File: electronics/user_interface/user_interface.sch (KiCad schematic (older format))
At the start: 29 parts, among them J1 Conn_01x06, J2 Conn_02x05_Odd_Even, U1 PCF8574, U2 PCF8574

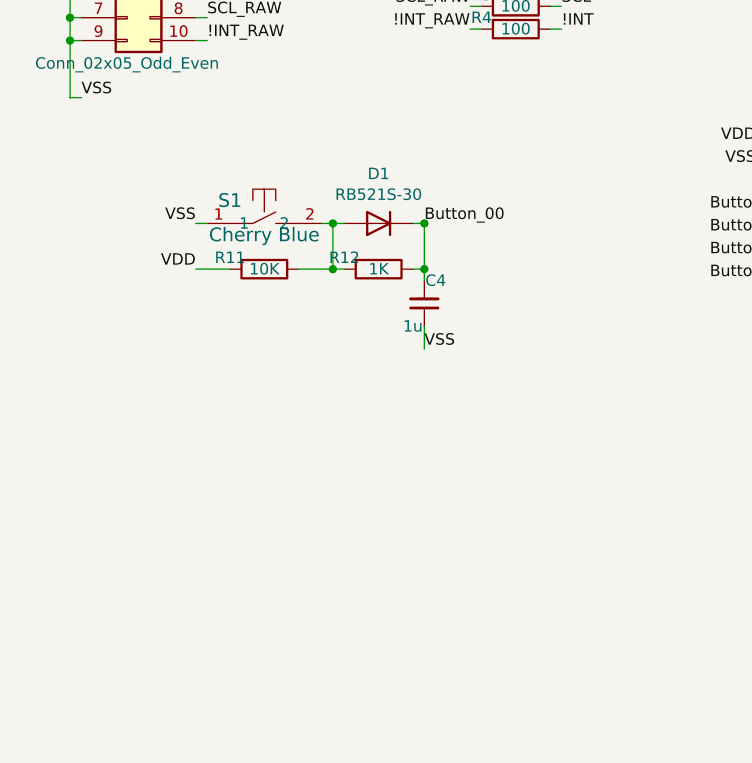
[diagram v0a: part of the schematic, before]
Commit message: added 3 switches extra to schematic
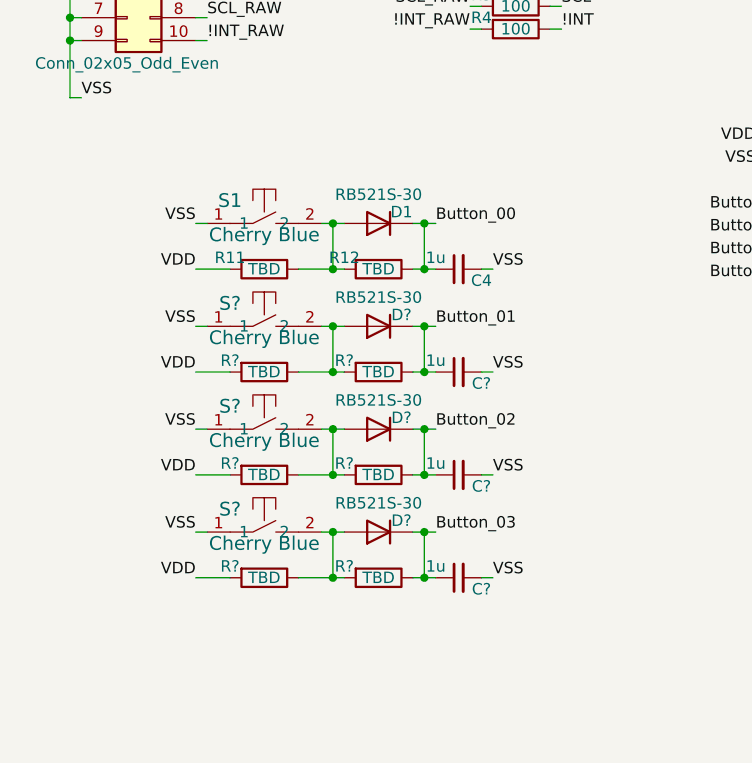
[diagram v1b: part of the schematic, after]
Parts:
- added C? (x3): 1u, SquantorRcl:C_0603, symbol Device:C_Small
- added D? (x3): RB521S-30, SquantorDiodes:SOD-523, symbol Device:D
- added R? (x6): TBD, SquantorRcl:R_0603_hand, symbol Device:R
- added S? (x3): Cherry Blue, MX_Only:MXOnly-1U-NoLED, symbol SquantorSwitches:2pin_tact_switch
- R11: value 10K -> TBD
- R12: value 1K -> TBD
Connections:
- net Button_00: now also C4.1; no longer C4.2
- net Button_01: now also C?.1, D?.1 (K), R?.1
- net Button_02: now also C?.1, D?.1 (K), R?.1
- net Button_03: now also C?.1, D?.1 (K), R?.1
- net VDD: now also R?.2, R?.2, R?.2
- net VSS: now also C4.2, C?.2, C?.2, C?.2, S?.1, S?.1, S?.1; no longer C4.1
- new net: D?.2 (A), R?.1, R?.2, S?.2 (x3)
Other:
- moved on the sheet: C4

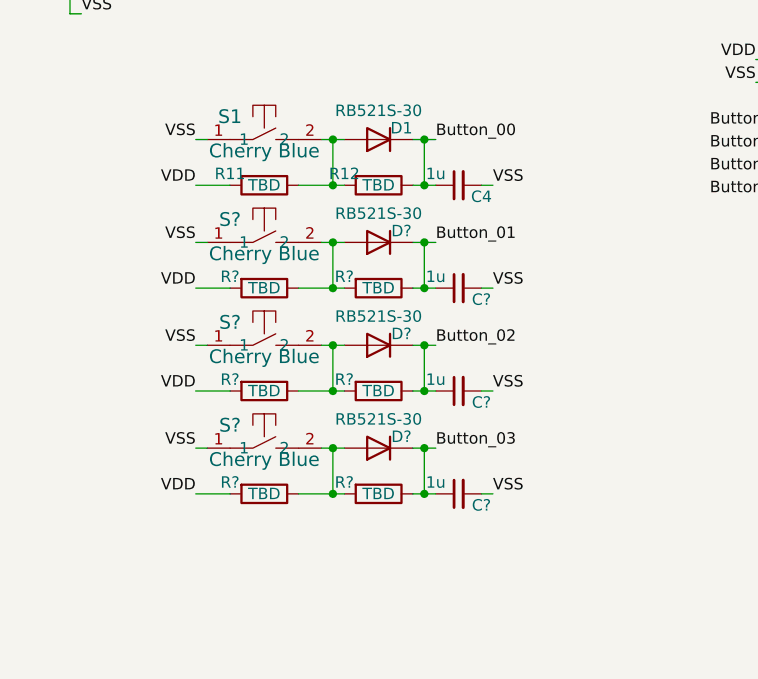
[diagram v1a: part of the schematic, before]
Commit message: minor silk and layout
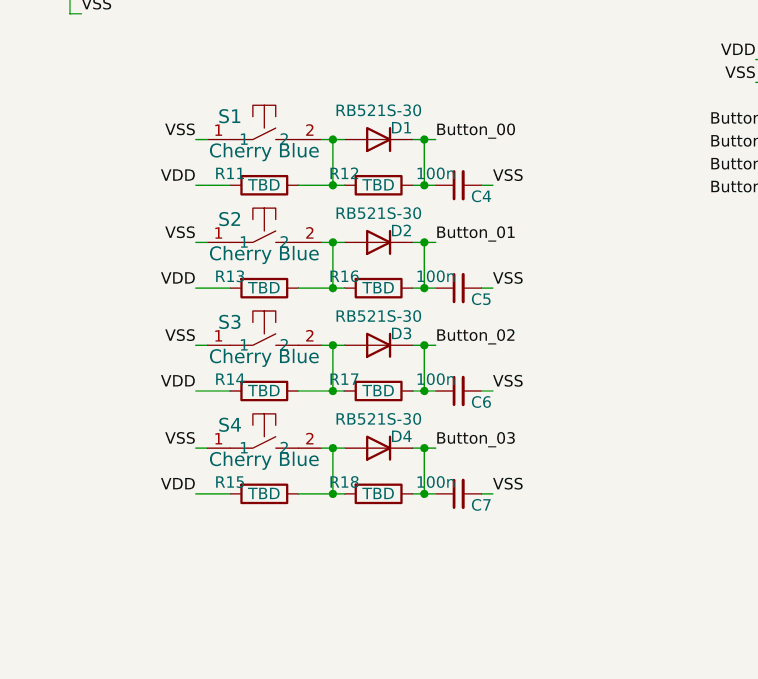
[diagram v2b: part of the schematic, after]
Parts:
- C4: value 1u -> 100n
- C5, C6, C7: renamed from C?; value 1u -> 100n
- gave numbers to parts that had none: 12
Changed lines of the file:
@@
 P 2500 3050
 F 0 "C4" V 2450 2950 50  0000 C CNN
-F 1 "1u" V 2550 3150 50  0000 C CNN
+F 1 "100n" V 2550 3150 50  0000 C CNN
 F 2 "SquantorRcl:C_0603" H 2500 3050 50  0001 C CNN
 F 3 "~" H 2500 3050 50  0001 C CNN
@@
 Connection ~ 2350 2850
 $Comp
-L SquantorSwitches:2pin_tact_switch S?
+L SquantorSwitches:2pin_tact_switch S2
 U 1 1 5EC685E5
 P 1650 3300
-F 0 "S?" H 1500 3400 60  0000 C CNN
+F 0 "S2" H 1500 3400 60  0000 C CNN
 F 1 "Cherry Blue" H 1650 3250 60  0000 C CNN
 F 2 "MX_Only:MXOnly-1U-NoLED" H 1650 3300 60  0001 C CNN
@@
 	1350 3300 1400 3300
 $Comp
-L Device:R R?
+L Device:R R16
 U 1 1 5EC685F1
 P 2150 3500
-F 0 "R?" V 2100 3350 50  0000 C CNN
+F 0 "R16" V 2100 3350 50  0000 C CNN
 F 1 "TBD" V 2150 3500 50  0000 C CNN
 F 2 "SquantorRcl:R_0603_hand" V 2080 3500 50  0001 C CNN
@@
 $EndComp
 $Comp
-L Device:R R?
+L Device:R R13
 U 1 1 5EC685FB
 P 1650 3500
-F 0 "R?" V 1600 3350 50  0000 C CNN
+F 0 "R13" V 1600 3350 50  0000 C CNN
 F 1 "TBD" V 1650 3500 50  0000 C CNN
 F 2 "SquantorRcl:R_0603_hand" V 1580 3500 50  0001 C CNN
@@
 	2000 3500 1950 3500
 $Comp
-L Device:C_Small C?
+L Device:C_Small C5
 U 1 1 5EC68608
 P 2500 3500
-F 0 "C?" V 2450 3400 50  0000 C CNN
-F 1 "1u" V 2550 3600 50  0000 C CNN
+F 0 "C5" V 2450 3400 50  0000 C CNN
+F 1 "100n" V 2550 3600 50  0000 C CNN
 F 2 "SquantorRcl:C_0603" H 2500 3500 50  0001 C CNN
 F 3 "~" H 2500 3500 50  0001 C CNN
@@
 	2600 3500 2650 3500
 $Comp
-L Device:D D?
+L Device:D D2
 U 1 1 5EC68616
 P 2150 3300
-F 0 "D?" H 2050 3250 50  0000 C CNN
+F 0 "D2" H 2050 3250 50  0000 C CNN
 F 1 "RB521S-30" H 2150 3174 50  0000 C CNN
 F 2 "SquantorDiodes:SOD-523" H 2150 3300 50  0001 C CNN
@@
 Connection ~ 2350 3300
 $Comp
-L SquantorSwitches:2pin_tact_switch S?
+L SquantorSwitches:2pin_tact_switch S3
 U 1 1 5EC702DD
 P 1650 3750
-F 0 "S?" H 1500 3850 60  0000 C CNN
+F 0 "S3" H 1500 3850 60  0000 C CNN
 F 1 "Cherry Blue" H 1650 3700 60  0000 C CNN
 F 2 "MX_Only:MXOnly-1U-NoLED" H 1650 3750 60  0001 C CNN
@@
 	1350 3750 1400 3750
 $Comp
-L Device:R R?
+L Device:R R17
 U 1 1 5EC702E9
 P 2150 3950
-F 0 "R?" V 2100 3800 50  0000 C CNN
+F 0 "R17" V 2100 3800 50  0000 C CNN
 F 1 "TBD" V 2150 3950 50  0000 C CNN
 F 2 "SquantorRcl:R_0603_hand" V 2080 3950 50  0001 C CNN
@@
 $EndComp
 $Comp
-L Device:R R?
+L Device:R R14
 U 1 1 5EC702F3
 P 1650 3950
-F 0 "R?" V 1600 3800 50  0000 C CNN
+F 0 "R14" V 1600 3800 50  0000 C CNN
 F 1 "TBD" V 1650 3950 50  0000 C CNN
 F 2 "SquantorRcl:R_0603_hand" V 1580 3950 50  0001 C CNN
@@
 	2000 3950 1950 3950
 $Comp
-L Device:C_Small C?
+L Device:C_Small C6
 U 1 1 5EC70300
 P 2500 3950
-F 0 "C?" V 2450 3850 50  0000 C CNN
-F 1 "1u" V 2550 4050 50  0000 C CNN
+F 0 "C6" V 2450 3850 50  0000 C CNN
+F 1 "100n" V 2550 4050 50  0000 C CNN
 F 2 "SquantorRcl:C_0603" H 2500 3950 50  0001 C CNN
 F 3 "~" H 2500 3950 50  0001 C CNN
@@
 	2600 3950 2650 3950
 $Comp
-L Device:D D?
+L Device:D D3
 U 1 1 5EC7030E
 P 2150 3750
-F 0 "D?" H 2050 3700 50  0000 C CNN
+F 0 "D3" H 2050 3700 50  0000 C CNN
 F 1 "RB521S-30" H 2150 3624 50  0000 C CNN
 F 2 "SquantorDiodes:SOD-523" H 2150 3750 50  0001 C CNN
@@
 Connection ~ 2350 3750
 $Comp
-L SquantorSwitches:2pin_tact_switch S?
+L SquantorSwitches:2pin_tact_switch S4
 U 1 1 5EC70324
 P 1650 4200
-F 0 "S?" H 1500 4300 60  0000 C CNN
+F 0 "S4" H 1500 4300 60  0000 C CNN
 F 1 "Cherry Blue" H 1650 4150 60  0000 C CNN
 F 2 "MX_Only:MXOnly-1U-NoLED" H 1650 4200 60  0001 C CNN
@@
 	1350 4200 1400 4200
 $Comp
-L Device:R R?
+L Device:R R18
 U 1 1 5EC70330
 P 2150 4400
-F 0 "R?" V 2100 4250 50  0000 C CNN
+F 0 "R18" V 2100 4250 50  0000 C CNN
 F 1 "TBD" V 2150 4400 50  0000 C CNN
 F 2 "SquantorRcl:R_0603_hand" V 2080 4400 50  0001 C CNN
@@
 $EndComp
 $Comp
-L Device:R R?
+L Device:R R15
 U 1 1 5EC7033A
 P 1650 4400
-F 0 "R?" V 1600 4250 50  0000 C CNN
+F 0 "R15" V 1600 4250 50  0000 C CNN
 F 1 "TBD" V 1650 4400 50  0000 C CNN
 F 2 "SquantorRcl:R_0603_hand" V 1580 4400 50  0001 C CNN
@@
 	2000 4400 1950 4400
 $Comp
-L Device:C_Small C?
+L Device:C_Small C7
 U 1 1 5EC70347
 P 2500 4400
-F 0 "C?" V 2450 4300 50  0000 C CNN
-F 1 "1u" V 2550 4500 50  0000 C CNN
+F 0 "C7" V 2450 4300 50  0000 C CNN
+F 1 "100n" V 2550 4500 50  0000 C CNN
 F 2 "SquantorRcl:C_0603" H 2500 4400 50  0001 C CNN
 F 3 "~" H 2500 4400 50  0001 C CNN
@@
 	2600 4400 2650 4400
 $Comp
-L Device:D D?
+L Device:D D4
 U 1 1 5EC70355
 P 2150 4200
-F 0 "D?" H 2050 4150 50  0000 C CNN
+F 0 "D4" H 2050 4150 50  0000 C CNN
 F 1 "RB521S-30" H 2150 4074 50  0000 C CNN
 F 2 "SquantorDiodes:SOD-523" H 2150 4200 50  0001 C CNN

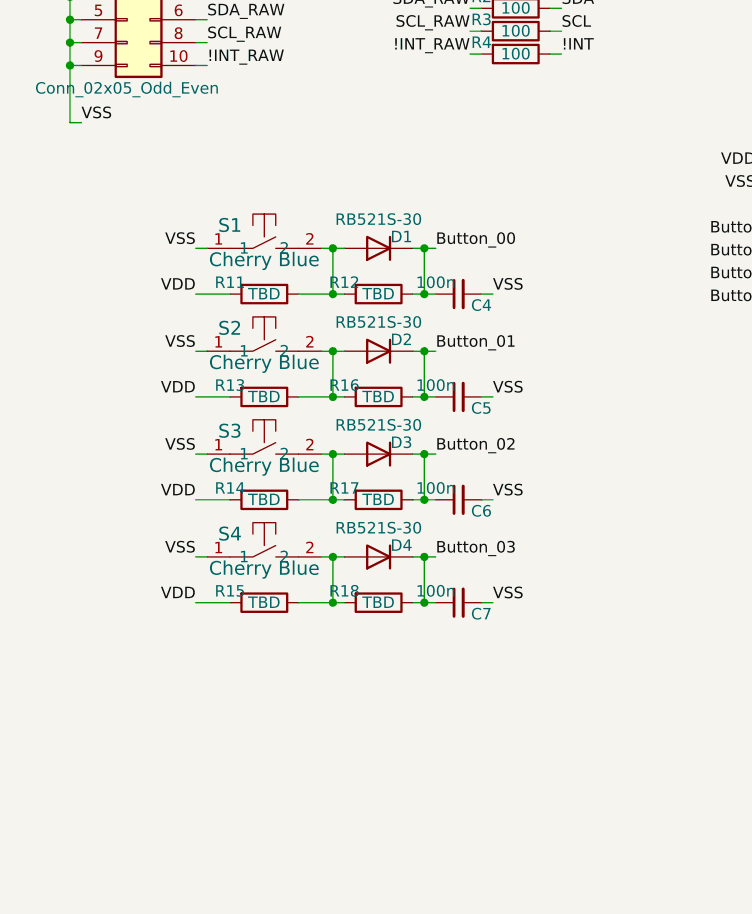
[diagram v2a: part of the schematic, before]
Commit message: added ESD protection
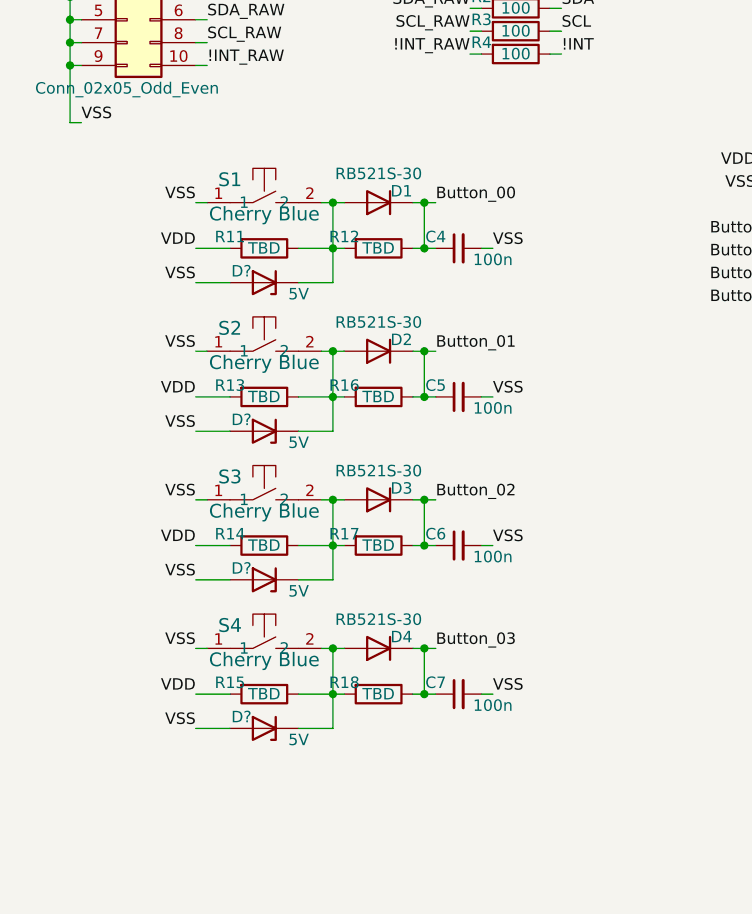
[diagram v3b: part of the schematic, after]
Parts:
- added D? (x4): 5V, SquantorDiodes:SOD-523, symbol Device:D_Zener
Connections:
- net VSS: now also D?.2 (A), D?.2 (A), D?.2 (A), D?.2 (A)
- net at D1.2 (A), R11.1, R12.2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: now also D?.1 (K)
- net at D2.2 (A), R13.1, R16.2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: now also D?.1 (K)
- net at D3.2 (A), R14.1, R17.2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: now also D?.1 (K)
- net at D4.2 (A), R15.1, R18.2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: now also D?.1 (K)
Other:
- moved on the sheet: C4, C6, C7, D1, D3, D4, R11, R12, R14, R15, R17, R18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

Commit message: assigned names to diodes
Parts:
- gave numbers to parts that had none: 4
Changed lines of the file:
@@
 Connection ~ 2350 4600
 $Comp
-L Device:D_Zener D?
+L Device:D_Zener D5
 U 1 1 5ECC2688
 P 1650 3000
-F 0 "D?" H 1750 2950 50  0000 C CNN
+F 0 "D5" H 1750 2950 50  0000 C CNN
 F 1 "5V" H 1500 3050 50  0000 C CNN
 F 2 "SquantorDiodes:SOD-523" H 1650 3000 50  0001 C CNN
@@
 	1500 3000 1350 3000
 $Comp
-L Device:D_Zener D?
+L Device:D_Zener D6
 U 1 1 5ED07DE5
 P 1650 3650
-F 0 "D?" H 1750 3600 50  0000 C CNN
+F 0 "D6" H 1750 3600 50  0000 C CNN
 F 1 "5V" H 1500 3700 50  0000 C CNN
 F 2 "SquantorDiodes:SOD-523" H 1650 3650 50  0001 C CNN
@@
 	1500 3650 1350 3650
 $Comp
-L Device:D_Zener D?
+L Device:D_Zener D7
 U 1 1 5ED187C7
 P 1650 4300
-F 0 "D?" H 1750 4250 50  0000 C CNN
+F 0 "D7" H 1750 4250 50  0000 C CNN
 F 1 "5V" H 1500 4350 50  0000 C CNN
 F 2 "SquantorDiodes:SOD-523" H 1650 4300 50  0001 C CNN
@@
 	1500 4300 1350 4300
 $Comp
-L Device:D_Zener D?
+L Device:D_Zener D8
 U 1 1 5ED2BAE1
 P 1650 4950
-F 0 "D?" H 1750 4900 50  0000 C CNN
+F 0 "D8" H 1750 4900 50  0000 C CNN
 F 1 "5V" H 1500 5000 50  0000 C CNN
 F 2 "SquantorDiodes:SOD-523" H 1650 4950 50  0001 C CNN
